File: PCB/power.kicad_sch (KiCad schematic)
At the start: 51 parts, among them Q1 AO3401A, U5 LM317_SOT-223, U6 LM317_SOT-223, U7 TPS65131RGE, U8 LM317_SOT-223, U9 LM337_SOT223

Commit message: Added WE inductor for power. Library is attached to project for reference
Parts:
- L1, L2: footprint (none) -> LIB:WE-MAPI_4030; Mfg (none) -> Würth Elektronik; Mfg Partnumber (none) -> 74438357047
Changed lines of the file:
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@@
 	)
 	(symbol
+		(lib_id "Device:L")
+		(at 156.21 76.2 180)
+		(unit 1)
+		(exclude_from_sim no)
+		(in_bom yes)
+		(on_board yes)
+		(dnp no)
+		(fields_autoplaced yes)
+		(property "Reference" "L2"
+			(at 157.48 74.9299 0)
+			(effects
+				(font
+					(size 1.27 1.27)
+				)
+				(justify right)
+			)
+		)
+		(property "Value" "4.7uH"
+			(at 157.48 77.4699 0)
+			(effects
+				(font
+					(size 1.27 1.27)
+				)
+				(justify right)
+			)
+		)
+		(property "Footprint" "LIB:WE-MAPI_4030"
+			(at 156.21 76.2 0)
+			(effects
+				(font
+					(size 1.27 1.27)
+				)
+				(hide yes)
+			)
+		)
+		(property "Datasheet" "https://www.we-online.com/components/products/datasheet/74438357047.pdf"
+			(at 156.21 76.2 0)
+			(effects
+				(font
+					(size 1.27 1.27)
+				)
+				(hide yes)
+			)
+		)
+		(property "Description" "Inductor"
+			(at 156.21 76.2 0)
+			(effects
+				(font
+					(size 1.27 1.27)
+				)
+				(hide yes)
+			)
+		)
+		(property "Mfg Partnumber" "74438357047"
+			(at 156.21 76.2 90)
+			(effects
+				(font
+					(size 1.27 1.27)
+				)
+				(hide yes)
+			)
+		)
+		(property "Mfg" "Würth Elektronik"
+			(at 156.21 76.2 90)
+			(effects
+				(font
+					(size 1.27 1.27)
+				)
+				(hide yes)
+			)
+		)
+		(pin "1"
+		)
+		(pin "2"
+		)
+		(instances
+			(project "mhd314"
+				(path "/afee45fc-2361-4efb-9cde-757fc2efd57b/b0c3c96c-8419-4ffd-8e63-3926f4c1a6a6"
+					(reference "L2")
+					(unit 1)
+				)
+			)
+		)
+	)
+	(symbol
 		(lib_id "Regulator_Linear:LM317_SOT-223")
 		(at 73.66 158.75 0)
@@
 	)
 	(symbol
-		(lib_id "Device:L")
-		(at 156.21 76.2 180)
-		(unit 1)
-		(exclude_from_sim no)
-		(in_bom yes)
-		(on_board yes)
-		(dnp no)
-		(fields_autoplaced yes)
-		(property "Reference" "L2"
-			(at 157.48 74.9299 0)
-			(effects
-				(font
-					(size 1.27 1.27)
-				)
-				(justify right)
-			)
-		)
-		(property "Value" "4.7uH"
-			(at 157.48 77.4699 0)
-			(effects
-				(font
-					(size 1.27 1.27)
-				)
-				(justify right)
-			)
-		)
-		(property "Footprint" ""
-			(at 156.21 76.2 0)
-			(effects
-				(font
-					(size 1.27 1.27)
-				)
-				(hide yes)
-			)
-		)
-		(property "Datasheet" "~"
-			(at 156.21 76.2 0)
-			(effects
-				(font
-					(size 1.27 1.27)
-				)
-				(hide yes)
-			)
-		)
-		(property "Description" "Inductor"
-			(at 156.21 76.2 0)
-			(effects
-				(font
-					(size 1.27 1.27)
-				)
-				(hide yes)
-			)
-		)
-		(pin "1"
-		)
-		(pin "2"
-		)
-		(instances
-			(project "mhd314"
-				(path "/afee45fc-2361-4efb-9cde-757fc2efd57b/b0c3c96c-8419-4ffd-8e63-3926f4c1a6a6"
-					(reference "L2")
-					(unit 1)
-				)
-			)
-		)
-	)
-	(symbol
 		(lib_id "power:VBUS")
 		(at 40.64 27.94 0)
@@
 			)
 		)
-		(property "Footprint" ""
+		(property "Footprint" "LIB:WE-MAPI_4030"
 			(at 85.09 33.02 0)
 			(effects
@@
 			)
 		)
-		(property "Datasheet" "~"
+		(property "Datasheet" "https://www.we-online.com/components/products/datasheet/74438357047.pdf"
 			(at 85.09 33.02 0)
 			(effects
@@
 			(effects
 				(font
+					(size 1.27 1.27)
+				)
+				(hide yes)
+			)
+		)
+		(property "Mfg Partnumber" "74438357047"
+			(at 85.09 33.02 90)
+			(effects
+				(font
+					(size 1.27 1.27)
+				)
+				(hide yes)
+			)
+		)
+		(property "Mfg" "Würth Elektronik"
+			(at 85.09 33.02 90)
+			(effects
+				(font

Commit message: Added E2P and testpoints
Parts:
- C22, C29, C48, C49: footprint Capacitor_SMD:C_0603_1608Metric_Pad1.08x0.95mm_HandSolder -> Capacitor_SMD:C_0402_1005Metric_Pad0.74x0.62mm_HandSolder
- C37, C40: footprint (none) -> Capacitor_SMD:C_0603_1608Metric_Pad1.08x0.95mm_HandSolder
- C38, C41, C42, C43, C44, C45: footprint (none) -> Capacitor_SMD:C_0402_1005Metric_Pad0.74x0.62mm_HandSolder
- R43, R44, R53, R54, R55, R56, R57, R58, R59, R60, R61, R62, R63, R64, R65, R66, R67, R68, R69, R70: footprint (none) -> Resistor_SMD:R_0402_1005Metric_Pad0.72x0.64mm_HandSolder
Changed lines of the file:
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@@
 			)
 		)
-		(property "Footprint" "Capacitor_SMD:C_0603_1608Metric_Pad1.08x0.95mm_HandSolder"
+		(property "Footprint" "Capacitor_SMD:C_0402_1005Metric_Pad0.74x0.62mm_HandSolder"
 			(at 205.4352 80.01 0)
 			(effects
@@
 			)
 		)
-		(property "Footprint" ""
+		(property "Footprint" "Capacitor_SMD:C_0402_1005Metric_Pad0.74x0.62mm_HandSolder"
 			(at 171.1452 41.91 0)
 			(effects
@@
 			)
 		)
-		(property "Footprint" ""
+		(property "Footprint" "Resistor_SMD:R_0402_1005Metric_Pad0.72x0.64mm_HandSolder"
 			(at 147.32 150.622 90)
 			(effects
@@
 			)
 		)
-		(property "Footprint" ""
+		(property "Footprint" "Capacitor_SMD:C_0402_1005Metric_Pad0.74x0.62mm_HandSolder"
 			(at 125.4252 83.82 0)
 			(effects
@@
 			)
 		)
-		(property "Footprint" ""
+		(property "Footprint" "Resistor_SMD:R_0402_1005Metric_Pad0.72x0.64mm_HandSolder"
 			(at 158.242 48.26 90)
 			(effects
@@
 			)
 		)
-		(property "Footprint" ""
+		(property "Footprint" "Resistor_SMD:R_0402_1005Metric_Pad0.72x0.64mm_HandSolder"
 			(at 223.012 54.61 90)
 			(effects
@@
 			)
 		)
-		(property "Footprint" ""
+		(property "Footprint" "Resistor_SMD:R_0402_1005Metric_Pad0.72x0.64mm_HandSolder"
 			(at 147.32 133.858 90)
 			(effects
@@
 			)
 		)
-		(property "Footprint" ""
+		(property "Footprint" "Resistor_SMD:R_0402_1005Metric_Pad0.72x0.64mm_HandSolder"
 			(at 147.32 123.698 90)
 			(effects
@@
 			)
 		)
-		(property "Footprint" ""
+		(property "Footprint" "Resistor_SMD:R_0402_1005Metric_Pad0.72x0.64mm_HandSolder"
 			(at 88.392 163.83 90)
 			(effects
@@
 			)
 		)
-		(property "Footprint" "Capacitor_SMD:C_0603_1608Metric_Pad1.08x0.95mm_HandSolder"
+		(property "Footprint" "Capacitor_SMD:C_0402_1005Metric_Pad0.74x0.62mm_HandSolder"
 			(at 56.8452 167.64 0)
 			(effects
@@
 			)
 		)
-		(property "Footprint" ""
+		(property "Footprint" "Capacitor_SMD:C_0402_1005Metric_Pad0.74x0.62mm_HandSolder"
 			(at 144.4752 67.31 0)
 			(effects
@@
 			)
 		)
-		(property "Footprint" ""
+		(property "Footprint" "Resistor_SMD:R_0402_1005Metric_Pad0.72x0.64mm_HandSolder"
 			(at 88.392 118.11 90)
 			(effects
@@
 			)
 		)
-		(property "Footprint" ""
+		(property "Footprint" "Resistor_SMD:R_0402_1005Metric_Pad0.72x0.64mm_HandSolder"
 			(at 54.61 24.638 90)
 			(effects
@@
 			)
 		)
-		(property "Footprint" ""
+		(property "Footprint" "Resistor_SMD:R_0402_1005Metric_Pad0.72x0.64mm_HandSolder"
 			(at 147.32 111.252 90)
 			(effects
@@
 			)
 		)
-		(property "Footprint" ""
+		(property "Footprint" "Resistor_SMD:R_0402_1005Metric_Pad0.72x0.64mm_HandSolder"
 			(at 147.32 173.228 90)
 			(effects
@@
 			)
 		)
-		(property "Footprint" ""
+		(property "Footprint" "Resistor_SMD:R_0402_1005Metric_Pad0.72x0.64mm_HandSolder"
 			(at 131.572 63.5 90)
 			(effects
@@
 			)
 		)
-		(property "Footprint" ""
+		(property "Footprint" "Capacitor_SMD:C_0402_1005Metric_Pad0.74x0.62mm_HandSolder"
 			(at 61.9252 71.12 0)
 			(effects
@@
 			)
 		)
-		(property "Footprint" ""
+		(property "Footprint" "Capacitor_SMD:C_0603_1608Metric_Pad1.08x0.95mm_HandSolder"
 			(at 69.5452 40.64 0)
 			(effects
@@
 			)
 		)
-		(property "Footprint" ""
+		(property "Footprint" "Resistor_SMD:R_0402_1005Metric_Pad0.72x0.64mm_HandSolder"
 			(at 71.882 172.72 90)
 			(effects
@@
 			)
 		)
-		(property "Footprint" ""
+		(property "Footprint" "Capacitor_SMD:C_0603_1608Metric_Pad1.08x0.95mm_HandSolder"
 			(at 41.6052 71.12 0)
 			(effects
@@
 			)
 		)
-		(property "Footprint" ""
+		(property "Footprint" "Resistor_SMD:R_0402_1005Metric_Pad0.72x0.64mm_HandSolder"
 			(at 147.32 163.068 90)
 			(effects
@@
 			)
 		)
-		(property "Footprint" ""
+		(property "Footprint" "Capacitor_SMD:C_0402_1005Metric_Pad0.74x0.62mm_HandSolder"
 			(at 148.59 51.1048 0)
 			(effects
@@
 			)
 		)
-		(property "Footprint" ""
+		(property "Footprint" "Resistor_SMD:R_0402_1005Metric_Pad0.72x0.64mm_HandSolder"
 			(at 49.53 61.468 90)
 			(effects
@@
 			)
 		)
-		(property "Footprint" ""
+		(property "Footprint" "Resistor_SMD:R_0402_1005Metric_Pad0.72x0.64mm_HandSolder"
 			(at 239.522 63.5 90)
 			(effects
@@
 			)
 		)
-		(property "Footprint" ""
+		(property "Footprint" "Resistor_SMD:R_0402_1005Metric_Pad0.72x0.64mm_HandSolder"
 			(at 158.242 38.1 90)
 			(effects
@@
 			)
 		)
-		(property "Footprint" ""
+		(property "Footprint" "Resistor_SMD:R_0402_1005Metric_Pad0.72x0.64mm_HandSolder"
 			(at 71.882 127 90)
 			(effects
@@
 			)
 		)
-		(property "Footprint" "Capacitor_SMD:C_0603_1608Metric_Pad1.08x0.95mm_HandSolder"
+		(property "Footprint" "Capacitor_SMD:C_0402_1005Metric_Pad0.74x0.62mm_HandSolder"
 			(at 201.6252 41.91 0)
 			(effects
@@
 			)
 		)
-		(property "Footprint" ""
+		(property "Footprint" "Capacitor_SMD:C_0402_1005Metric_Pad0.74x0.62mm_HandSolder"
 			(at 119.0752 83.82 0)
 			(effects
@@
 			)
 		)
-		(property "Footprint" "Capacitor_SMD:C_0603_1608Metric_Pad1.08x0.95mm_HandSolder"
+		(property "Footprint" "Capacitor_SMD:C_0402_1005Metric_Pad0.74x0.62mm_HandSolder"
 			(at 56.8452 121.92 0)
 			(effects
@@
 			)
 		)
-		(property "Footprint" ""
+		(property "Footprint" "Resistor_SMD:R_0402_1005Metric_Pad0.72x0.64mm_HandSolder"
 			(at 131.572 55.88 90)
 			(effects
@@
 			)
 		)
-		(property "Footprint" ""
+		(property "Footprint" "Resistor_SMD:R_0402_1005Metric_Pad0.72x0.64mm_HandSolder"
 			(at 223.012 45.72 90)
 			(effects
@@
 			)
 		)
-		(property "Footprint" ""
+		(property "Footprint" "Resistor_SMD:R_0402_1005Metric_Pad0.72x0.64mm_HandSolder"
 			(at 239.522 36.83 90)
 			(effects

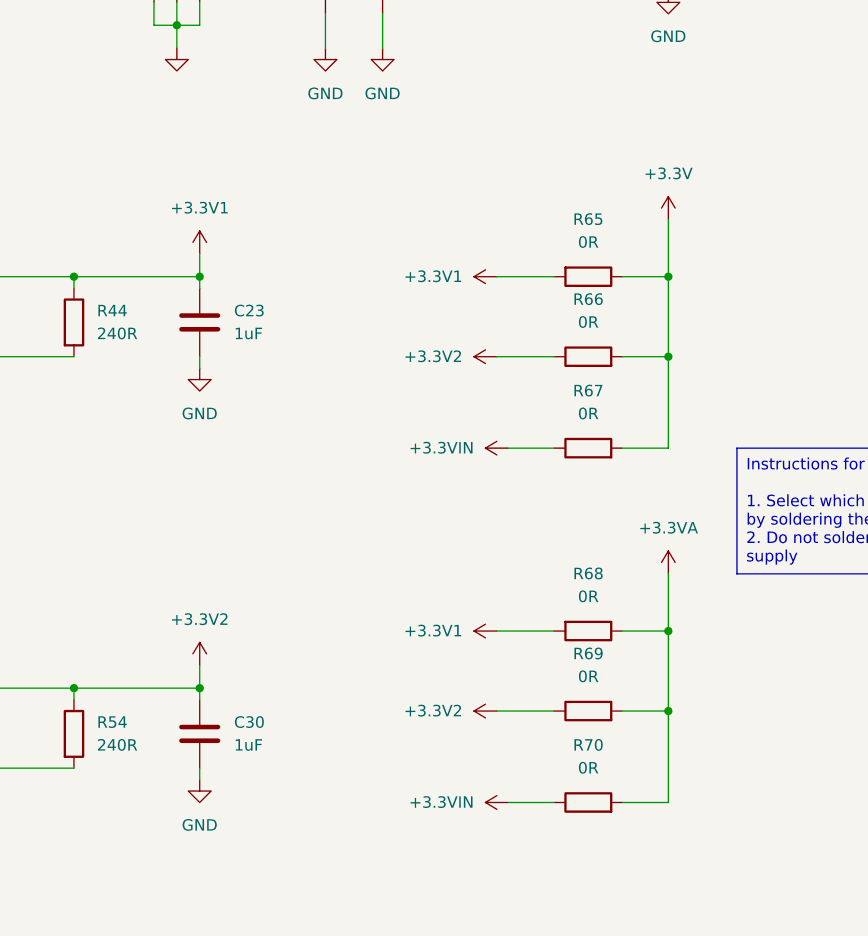
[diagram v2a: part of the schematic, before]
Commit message: Finished basic placement
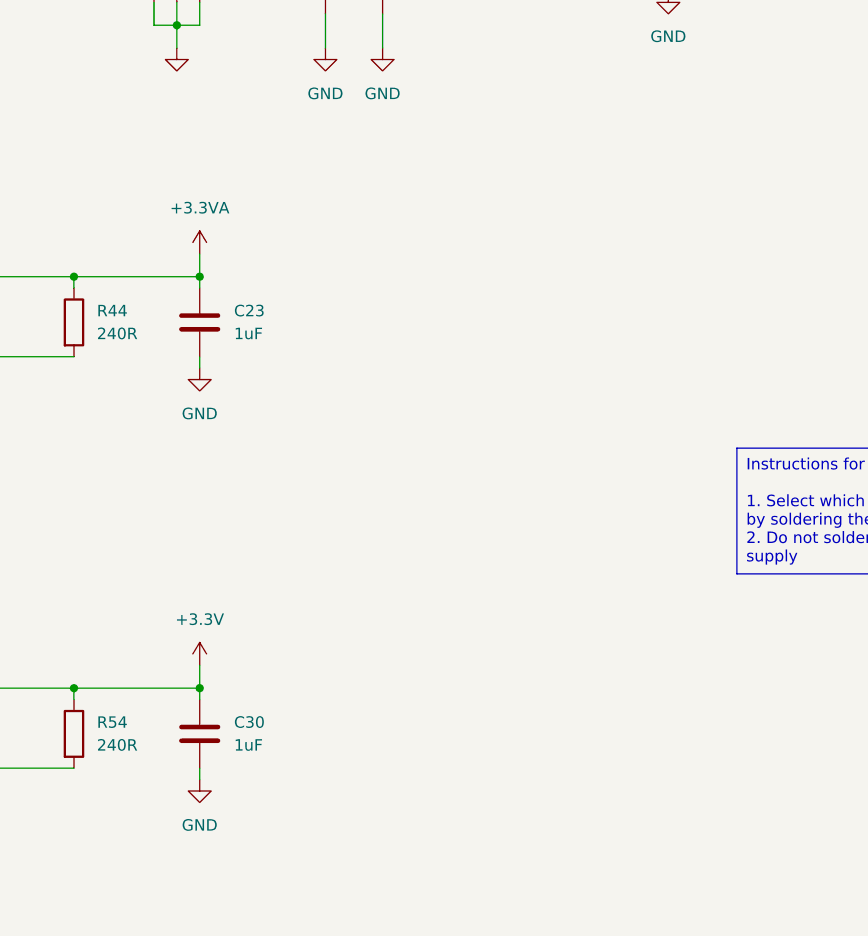
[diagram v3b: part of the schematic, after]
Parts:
- removed R65, R66, R67, R68, R69, R70: 0R, Resistor_SMD:R_0402_1005Metric_Pad0.72x0.64mm_HandSolder, symbol Device:R
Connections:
- net +3.3V1 is gone; now on net +3.3VA: C23.1, R44.1, U5.2 (VO)
- net +3.3V2 is gone; now on net +3.3V: C30.1, R54.1, U6.2 (VO)

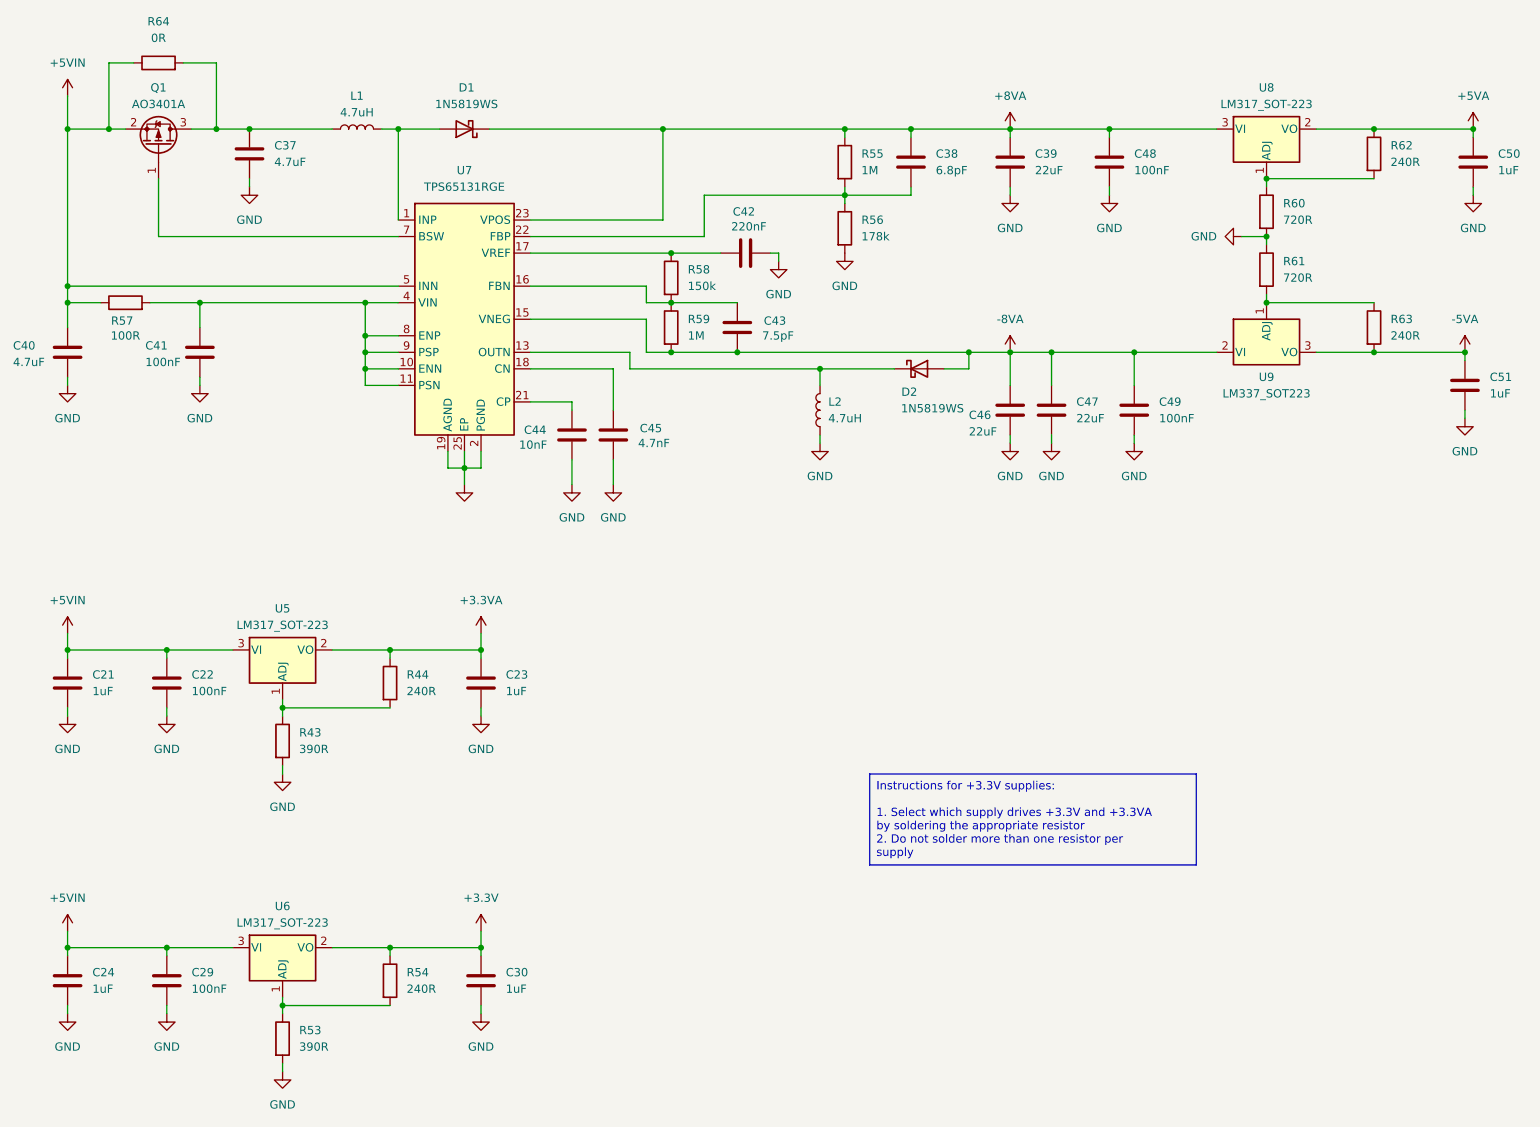
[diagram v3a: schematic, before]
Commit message: Routed power section
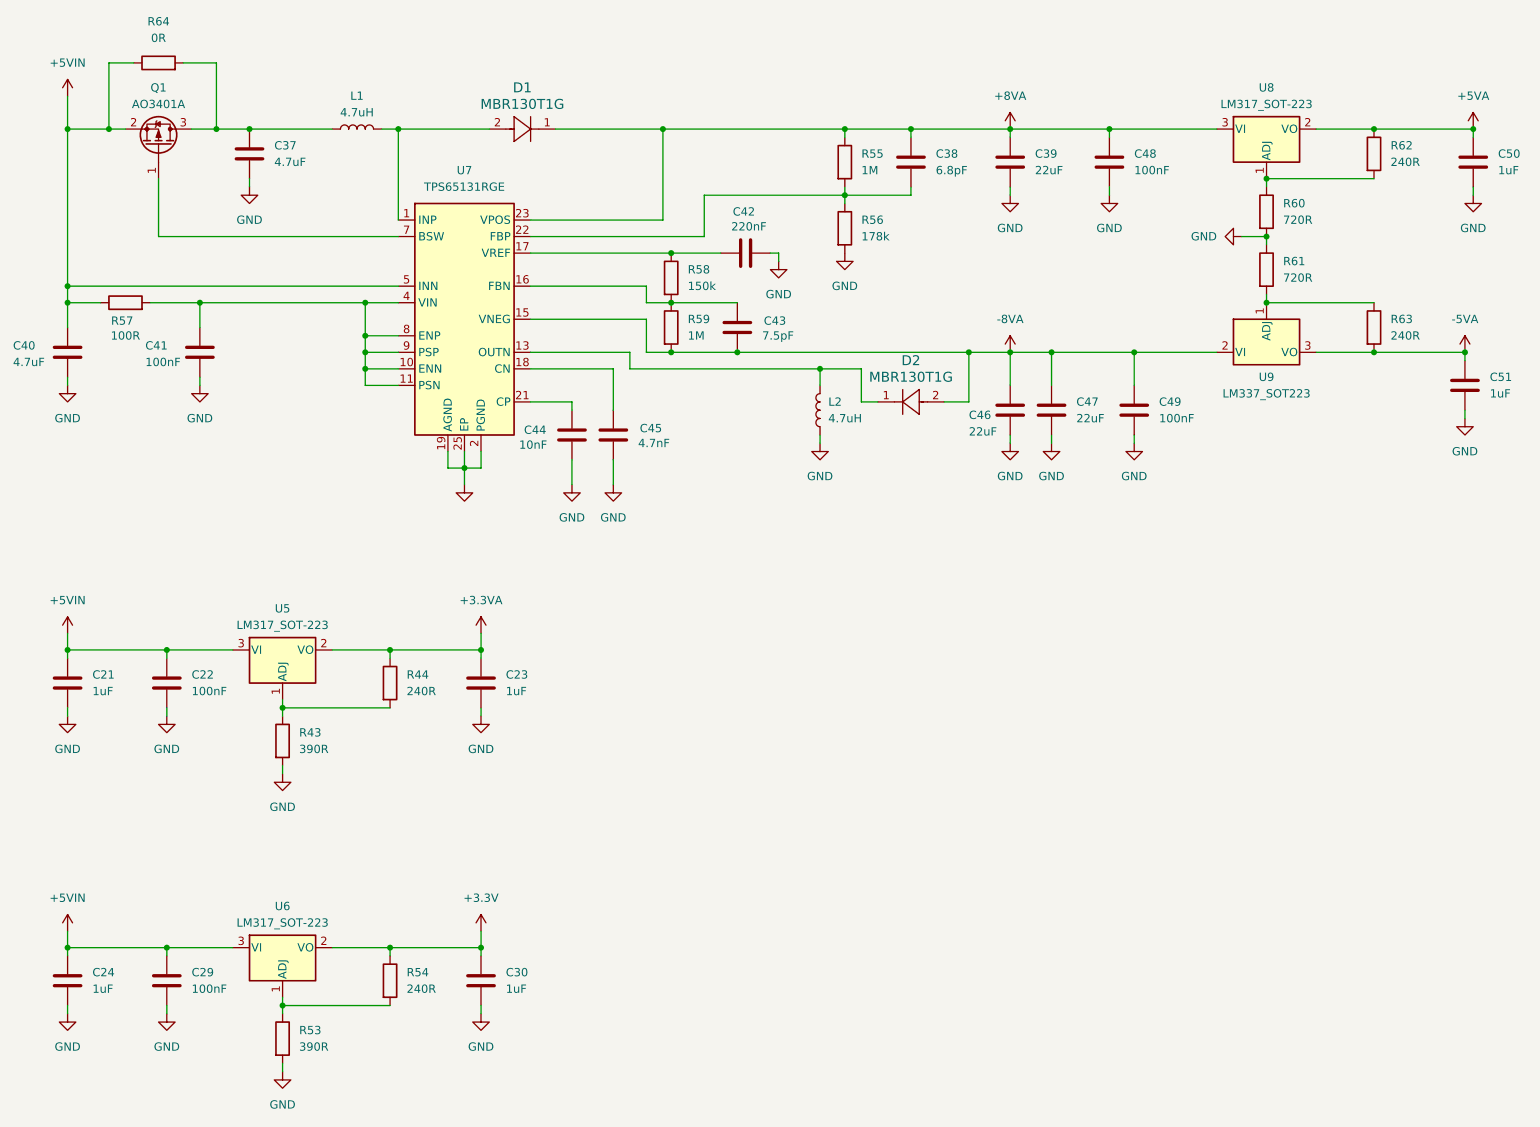
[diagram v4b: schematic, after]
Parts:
- removed D1, D2: 1N5819WS, Diode_SMD:D_SOD-323, symbol Diode:1N5819WS
- added D1, D2: MBR130T1G, SOD-123_425-04_ONS, symbol mahaudio_kicad_lib:MBR130T1G
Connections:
- net +8VA: now also D1.1
- net -8VA: now also D2.2
- net at L2.2, U7.13 (OUTN), U7.14 (OUTN): now also D2.1
- net at L1.2, U7.1 (INP), U7.24 (INP): now also D1.2
